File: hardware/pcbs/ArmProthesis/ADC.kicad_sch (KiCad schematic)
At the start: 27 parts, among them J2 H_16_2.54mm, SW1 SW_Reed_SPDT, SW2 SW_Reed_SPDT, SW3 SW_Reed_SPDT, SW4 SW_Reed_SPDT, U1 AD7606BSTZ

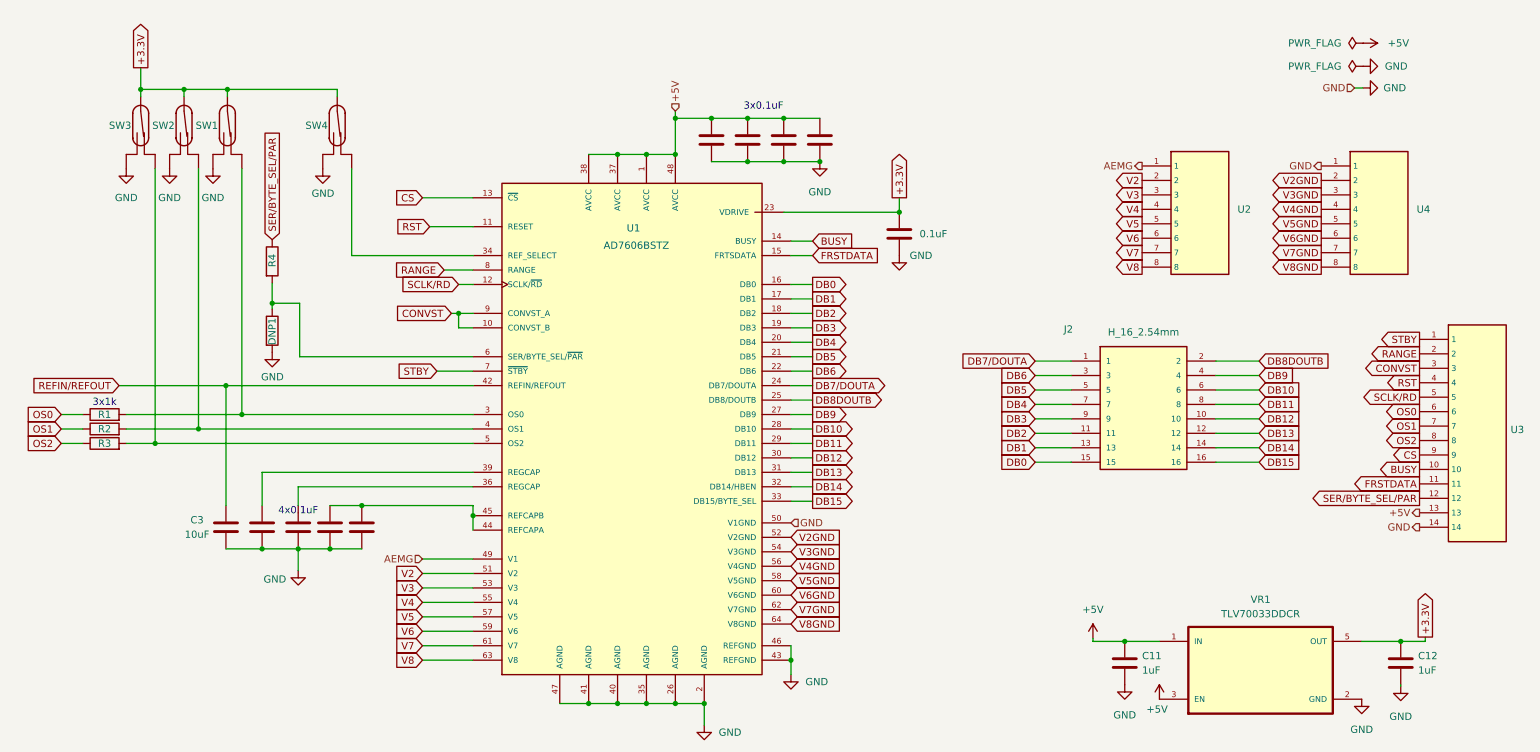
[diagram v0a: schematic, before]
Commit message: ADC + sEMG changes
sEMG - connector updates
ADC - major changes - connectors, layout changes
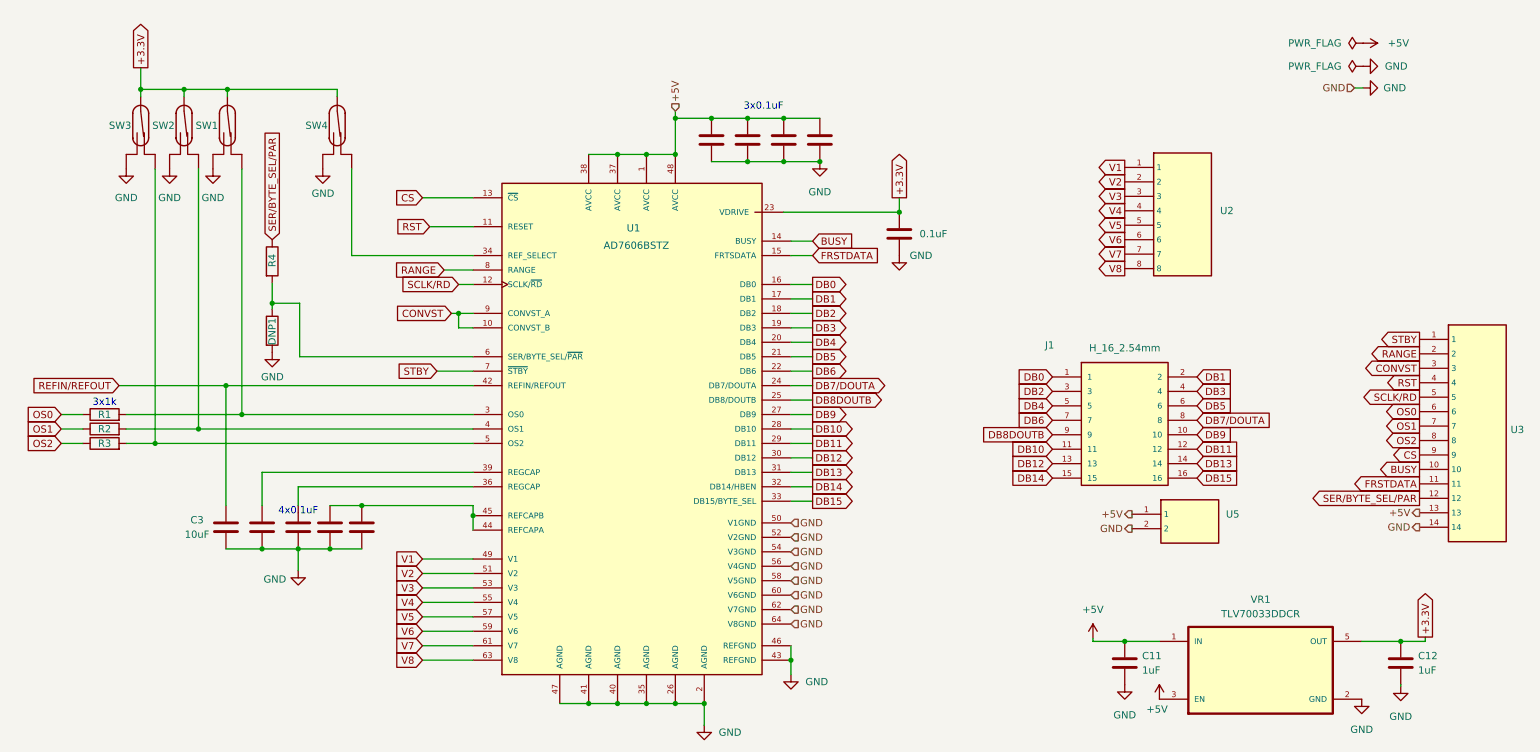
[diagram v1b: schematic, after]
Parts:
- removed J2: H_16_2.54mm, Connector_PinHeader_2.54mm:PinHeader_2x08_P2.54mm_Vertical, symbol headers:MTSW-150-22-S-D-415
- removed U4: ~, Connector_PinHeader_2.54mm:PinHeader_1x08_P2.54mm_Vertical, symbol headers:H_8
- added J1: H_16_2.54mm, Connector_JST:JST_SUR_SM16B-SURS-TF_1x16-1MP_P0.80mm_Horizontal, symbol headers:MTSW-150-22-S-D-415
- added U5: ~, Connector_JST:JST_GH_SM02B-GHS-TB_1x02-1MP_P1.25mm_Horizontal, symbol Headers:H_2
- U2: footprint Connector_PinHeader_2.54mm:PinHeader_1x08_P2.54mm_Vertical -> Connector_JST:JST_GH_SM08B-GHS-TB_1x08-1MP_P1.25mm_Horizontal
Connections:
- net V2GND is gone; now on net GND: U1.52 (V2GND)
- net V3GND is gone; now on net GND: U1.54 (V3GND)
- net V4GND is gone; now on net GND: U1.56 (V4GND)
- net V5GND is gone; now on net GND: U1.58 (V5GND)
- net V6GND is gone; now on net GND: U1.60 (V6GND)
- net V7GND is gone; now on net GND: U1.62 (V7GND)
- net V8GND is gone; now on net GND: U1.64 (V8GND)
- net +5V: now also U5.1
- net DB0: now also J1.1
- net DB1: now also J1.2
- net DB10: now also J1.11
- net DB11: now also J1.12
- net DB12: now also J1.13
- net DB13: now also J1.14
- net DB14: now also J1.15
- net DB15: now also J1.16
- net DB2: now also J1.3
- net DB3: now also J1.4
- net DB4: now also J1.5
- net DB5: now also J1.6
- net DB6: now also J1.7
- net DB7/DOUTA: now also J1.8
- net DB8DOUTB: now also J1.9
- net DB9: now also J1.10
- net GND: now also U5.2
- net AEMG renamed V1

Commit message: BMS v0.3 + main folder reconstruction
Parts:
- removed C1, C5: 0.1uF, Capacitor_SMD:C_0402_1005Metric_Pad0.74x0.62mm_HandSolder, symbol Device:C
- removed C10: 1uF, Capacitor_SMD:C_0402_1005Metric_Pad0.74x0.62mm_HandSolder, symbol Device:C
- added H1, H2, H3, H4: MountingHole, MountingHole:MountingHole_2.7mm_M2.5, symbol Mechanical:MountingHole
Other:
- moved on the sheet: C3

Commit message: updates
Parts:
- removed DNP1: 10-47k, Resistor_SMD:R_0805_2012Metric_Pad1.20x1.40mm_HandSolder, symbol Device:R
- removed H4: MountingHole, MountingHole:MountingHole_2.7mm_M2.5, symbol Mechanical:MountingHole
- removed SW4: SW_Reed_SPDT, Switches:switch1, symbol Switch:SW_Reed_SPDT
- removed U3: ~, Connector_PinHeader_2.54mm:PinHeader_1x14_P2.54mm_Vertical, symbol headers:H_14
- added J2: ~, Connector_PinHeader_2.54mm:PinHeader_1x12_P2.54mm_Vertical, symbol Connector_Generic:Conn_01x12
- added R5: 10k, Resistor_SMD:R_0603_1608Metric, symbol Device:R
- C11, C12, C2, C6: footprint Capacitor_SMD:C_0402_1005Metric_Pad0.74x0.62mm_HandSolder -> Capacitor_SMD:C_0402_1005Metric; LCSC (none) -> C167339
- C3: footprint Capacitor_SMD:C_0805_2012Metric_Pad1.18x1.45mm_HandSolder -> Capacitor_SMD:C_0603_1608Metric; LCSC (none) -> C19702
- C4, C8, C9: footprint Capacitor_SMD:C_0402_1005Metric_Pad0.74x0.62mm_HandSolder -> Capacitor_SMD:C_0402_1005Metric; LCSC (none) -> C141382
- C7: value 1uF -> 10 µF; footprint Capacitor_SMD:C_0402_1005Metric_Pad0.74x0.62mm_HandSolder -> Capacitor_SMD:C_0603_1608Metric; LCSC (none) -> C19702
- R1, R2, R3: footprint Resistor_SMD:R_0402_1005Metric_Pad0.72x0.64mm_HandSolder -> Resistor_SMD:R_0402_1005Metric; LCSC (none) -> C279981
- R4: value 1k -> 10k; footprint Resistor_SMD:R_0805_2012Metric_Pad1.20x1.40mm_HandSolder -> Resistor_SMD:R_0603_1608Metric; LCSC (none) -> C285206
- U1: Description_1 8-Channel DAS with 16-Bit, Bipolar Input, Simultaneous Sampling ADC -> 8-Channel DAS with 16-Bit, Bipolar Input, Simultaneous Sampling ADC; LCSC (none) -> C398827
- U2: LCSC (none) -> C265111
- U5: LCSC (none) -> C189893
- VR1: LCSC (none) -> C11337
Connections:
- net RANGE is gone; now on net GND: U1.8 (RANGE)
- net SER/BYTE_SEL/PAR is gone; now on net RST: R4.1
- net +3.3V: now also SW1.1, SW2.1, SW3.1, U1.34 (REF_SELECT); no longer SW1.2, SW2.2, SW3.2
- net +5V: now also J2.11 (Pin_11)
- net BUSY: now also J2.9 (Pin_9)
- net CONVST: now also J2.2 (Pin_2)
- net CS: now also J2.8 (Pin_8)
- net FRSTDATA: now also J2.10 (Pin_10)
- net GND: now also R4.2, U1.6 (SER/BYTE_SEL/~{PAR}), J2.12 (Pin_12), R5.2
- net OS0: now also J2.5 (Pin_5)
- net OS1: now also J2.6 (Pin_6)
- net OS2: now also J2.7 (Pin_7)
- net RST: now also J2.3 (Pin_3)
- net SCLK/RD: now also J2.4 (Pin_4)
- net STBY: now also J2.1 (Pin_1), R5.1
- net at R2.2, U1.4 (OS1): now also SW2.2; no longer SW2.1
- net at R1.2, U1.3 (OS0): now also SW1.2; no longer SW1.1
- net at R3.2, U1.5 (OS2): now also SW3.2; no longer SW3.1
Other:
- note removed: "3x0.1uF"
- moved on the sheet: SW1, SW2, SW3

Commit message: Ordered versions
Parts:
- removed J1: H_16_2.54mm, Connector_JST:JST_SUR_SM16B-SURS-TF_1x16-1MP_P0.80mm_Horizontal, symbol headers:MTSW-150-22-S-D-415
- added U3: OUT2, Connector_JST:JST_SH_SM08B-SRSS-TB_1x08-1MP_P1.00mm_Horizontal, symbol headers:H_8
- added U4: OUT1, Connector_JST:JST_SH_SM08B-SRSS-TB_1x08-1MP_P1.00mm_Horizontal, symbol headers:H_8
- C11, C12, C2, C6: LCSC C167339 -> C52923
- C4, C8, C9: LCSC C141382 -> C307331
- J2: value ~ -> SET; LCSC (none) -> C725944
- R1, R2, R3: LCSC C279981 -> C11702
- R4, R5: LCSC C285206 -> C25804
- SW1, SW2, SW3: footprint Switches:switch1 -> Button_Switch_SMD:SW_SPDT_Shouhan_MSK12C02; LCSC (none) -> C431540
- U2: value ~ -> IN
- U5: value ~ -> PWR
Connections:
- net DB0: now also U4.1
- net DB1: now also U4.2
- net DB10: now also U3.3
- net DB11: now also U3.4
- net DB12: now also U3.5
- net DB13: now also U3.6
- net DB14: now also U3.7
- net DB15: now also U3.8
- net DB2: now also U4.3
- net DB3: now also U4.4
- net DB4: now also U4.5
- net DB5: now also U4.6
- net DB6: now also U4.7
- net DB7/DOUTA: now also U4.8
- net DB8DOUTB: now also U3.1
- net DB9: now also U3.2
